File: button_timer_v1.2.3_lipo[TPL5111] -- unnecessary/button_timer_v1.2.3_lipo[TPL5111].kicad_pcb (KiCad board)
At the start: 2 copper layers, 21 x 41.7 mm, 25 parts, among them J1 Conn_01x05_Female, SW1 SW_Push, SW2 SW_Push, U2 AP2112K-3.3, U3 TPL5111, X1 ESP-12E

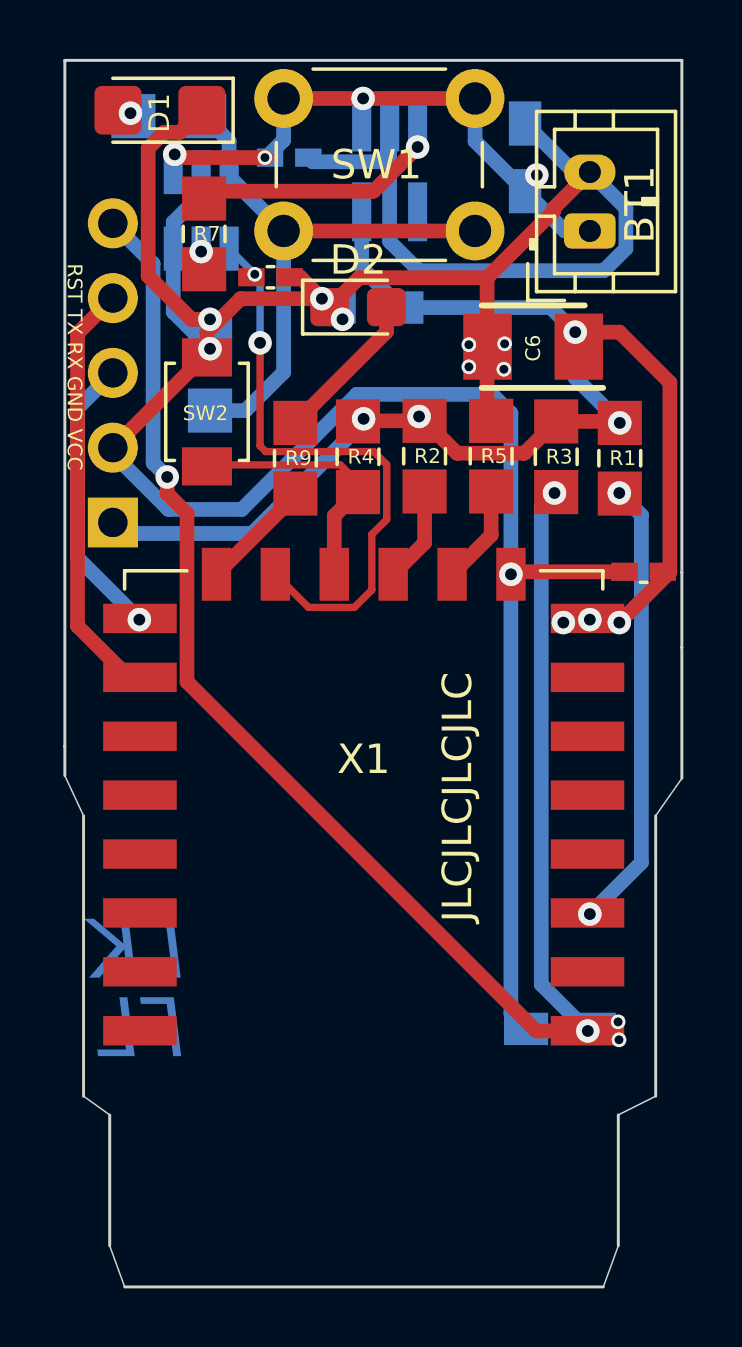
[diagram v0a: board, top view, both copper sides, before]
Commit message: Added 100nF decoupling capacitors between VCC and Ground of the ESP
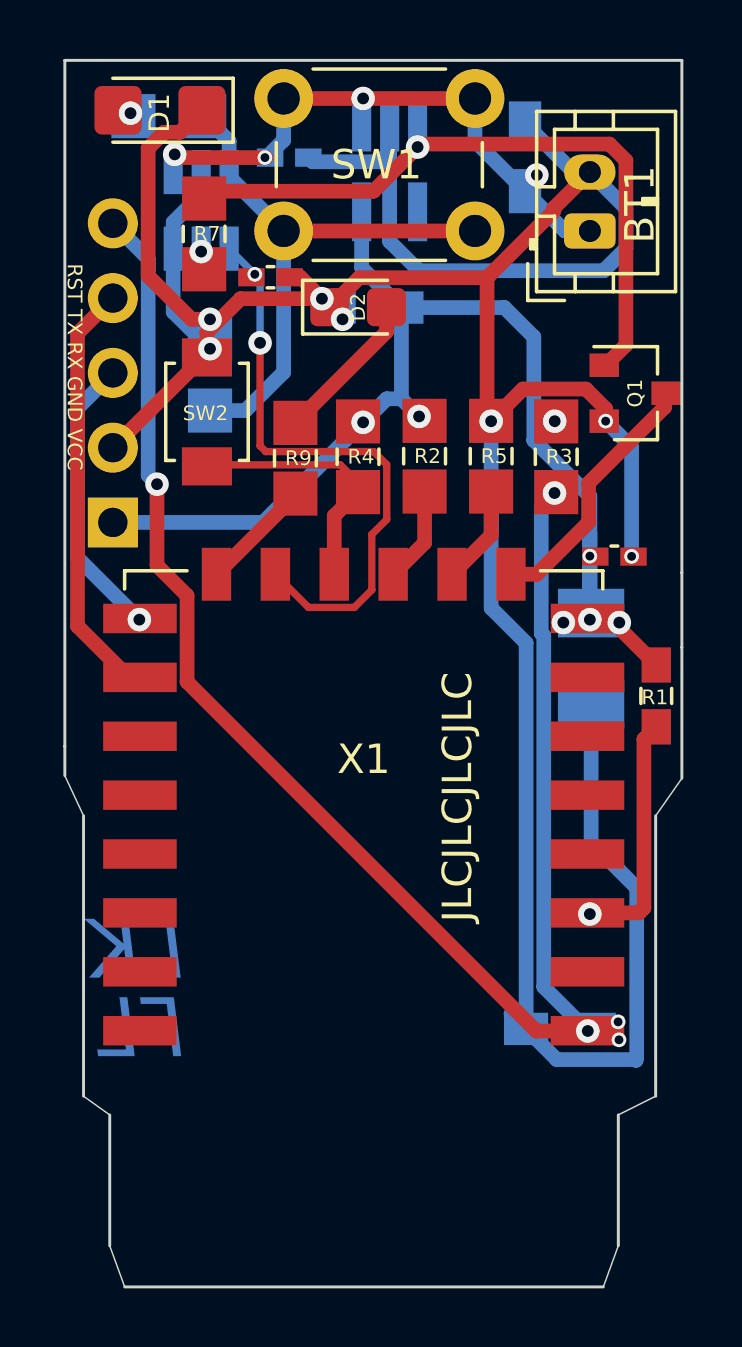
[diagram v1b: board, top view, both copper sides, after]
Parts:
- added Q1: mmbt2222, handsolder:SOT-23, F.Cu at (134.9, 72.0)
- C6: moved to B.Cu
- D2: footprint LED_SMD:LED_0805_2012Metric_Castellated -> handsolder:LED_0805_2012Metric_Castellated_mod
- R1: footprint handsolder:R_0805_2012handsoldermod -> handsolder:R_0603_1608Metric_Pad0.98x0.95mm_HandSolder_mod
- moved C6 10.8 mm to (133.4, 81.0), turned to 270 degrees
- moved R1 8.17 mm to (135.7, 82.3), turned to 90 degrees
- moved C7 1.12 mm to (134.2, 77.6), turned to 0 degrees
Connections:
- R1 pad 1: /VCC -> /EN
- R1 pad 2: /EN -> /VCC
- X1 pad 9: /GND -> /GND_ESP
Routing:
- net Net-(Q1-Pad1): track 8.05 -> 22.6 mm
- net /GND_ESP: track 0.00 -> 8.83 mm
- net /GND: track 107.2 -> 114.7 mm, vias 9 -> 7
- net /EN: track 15.5 -> 8.45 mm, vias 2 -> 1
- net /VCC: track 46.5 -> 41.4 mm
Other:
- board text added: "Button - LIPO v.1.2.3 TPL5111"
- board text added: "V1.2.3 ONLY LIPO TIMER TPL5111"
- board text removed: "Button - LIPO v.1.2.1"
- board text removed: "V1.2.1 ONLY LIPO TIMER TPL51111"
